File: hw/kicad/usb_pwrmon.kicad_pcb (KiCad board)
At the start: 2 copper layers, 31 parts, among them J1 ARM_10PIN, J2 USB_MALE_A, J3 USB_MICRO_B, J4 USB_FEMALE_A, SW1 SW_PUSH, U1 AD8293G80, U2 MKL24Z64VFM4

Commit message: - save
Former-commit-id: cf66670b65a8a882cb1622ef3f0bdfdf1408bc8a
Former-commit-id: 7a3e1ac5155b1945f7744ff238828485aaafe397
Former-commit-id: 743023cbd18d02b8dd289aac27cf0dd998f1e37a
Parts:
- moved J_2 6.27 mm to (85.9, 23.9)
- moved U2 5.92 mm to (91.9, 31.2), turned to 45 degrees
- moved U1 2.03 mm to (82.5, 28.7)
- moved R6 0.80 mm to (84.1, 35.1)
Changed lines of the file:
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@@
     (mod_text_size 1.5 1.5)
     (mod_text_width 0.15)
-    (pad_size 1.6 1.4)
-    (pad_drill 0)
+    (pad_size 3.4 3.4)
+    (pad_drill 2)
     (pad_to_mask_clearance 0.2)
     (aux_axis_origin 0 0)
@@
   )
   (module sot23-8 (layer F.Cu)
-    (at 84.582 28.702)
+    (at 82.55 28.702)
     (fp_text reference U1 (at 1.651 -1.397) (layer F.SilkS)
       (effects (font (size 0.75 0.75) (thickness 0.12)))
@@
   )
   (module oled_fpc_30 (layer F.Cu)
-    (at 91.694 26.162)
+    (at 85.852 23.876)
     (fp_text reference J_2 (at 0 3) (layer F.SilkS)
       (effects (font (size 0.75 0.75) (thickness 0.12)))
@@
   )
   (module MKL24Z64VFM4 (layer F.Cu)
-    (at 94.996 36.322)
-    (fp_text reference U2 (at 0 -6) (layer F.SilkS)
-      (effects (font (size 0.75 0.75) (thickness 0.12)))
-    )
-    (fp_text value MKL24Z64VFM4 (at 0 5) (layer F.SilkS) hide
+    (at 91.948 31.242 45)
+    (fp_text reference U2 (at 0 -6 45) (layer F.SilkS)
+      (effects (font (size 0.75 0.75) (thickness 0.12)))
+    )
+    (fp_text value MKL24Z64VFM4 (at 0 5 45) (layer F.SilkS) hide
       (effects (font (size 1 1) (thickness 0.15)))
     )
-    (pad 1 smd rect (at -2.475 -1.75) (size 0.85 0.3)
+    (pad 1 smd rect (at -2.475 -1.75 45) (size 0.85 0.3)
       (layers F.Cu F.Paste F.Mask)
       (net 36 Net-<U2-Pad1>)
     )
-    (pad 2 smd rect (at -2.475 -1.25) (size 0.85 0.3)
-      (layers F.Cu F.Paste F.Mask)
-      (net 7 GND)
-    )
-    (pad 3 smd rect (at -2.475 -0.75) (size 0.85 0.3)
+    (pad 2 smd rect (at -2.475 -1.25 45) (size 0.85 0.3)
+      (layers F.Cu F.Paste F.Mask)
+      (net 7 GND)
+    )
+    (pad 3 smd rect (at -2.475 -0.75 45) (size 0.85 0.3)
       (layers F.Cu F.Paste F.Mask)
       (net 28 Net-<R4-Pad2>)
     )
-    (pad 4 smd rect (at -2.475 -0.25) (size 0.85 0.3)
+    (pad 4 smd rect (at -2.475 -0.25 45) (size 0.85 0.3)
       (layers F.Cu F.Paste F.Mask)
       (net 29 Net-<R5-Pad2>)
     )
-    (pad 5 smd rect (at -2.475 0.25) (size 0.85 0.3)
+    (pad 5 smd rect (at -2.475 0.25 45) (size 0.85 0.3)
       (layers F.Cu F.Paste F.Mask)
       (net 2 +3.3v)
     )
-    (pad 6 smd rect (at -2.475 0.75) (size 0.85 0.3)
+    (pad 6 smd rect (at -2.475 0.75 45) (size 0.85 0.3)
       (layers F.Cu F.Paste F.Mask)
       (net 47 USB_VBUS)
     )
-    (pad 7 smd rect (at -2.475 1.25) (size 0.85 0.3)
+    (pad 7 smd rect (at -2.475 1.25 45) (size 0.85 0.3)
       (layers F.Cu F.Paste F.Mask)
       (net 2 +3.3v)
     )
-    (pad 8 smd rect (at -2.475 1.75) (size 0.85 0.3)
-      (layers F.Cu F.Paste F.Mask)
-      (net 7 GND)
-    )
-    (pad 17 smd rect (at 2.475 1.75) (size 0.85 0.3)
+    (pad 8 smd rect (at -2.475 1.75 45) (size 0.85 0.3)
+      (layers F.Cu F.Paste F.Mask)
+      (net 7 GND)
+    )
+    (pad 17 smd rect (at 2.475 1.75 45) (size 0.85 0.3)
       (layers F.Cu F.Paste F.Mask)
       (net 34 Net-<U2-Pad17>)
     )
-    (pad 18 smd rect (at 2.475 1.25) (size 0.85 0.3)
+    (pad 18 smd rect (at 2.475 1.25 45) (size 0.85 0.3)
       (layers F.Cu F.Paste F.Mask)
       (net 35 Net-<U2-Pad18>)
     )
-    (pad 19 smd rect (at 2.475 0.75) (size 0.85 0.3)
+    (pad 19 smd rect (at 2.475 0.75 45) (size 0.85 0.3)
       (layers F.Cu F.Paste F.Mask)
       (net 9 NRESET)
     )
-    (pad 20 smd rect (at 2.475 0.25) (size 0.85 0.3)
+    (pad 20 smd rect (at 2.475 0.25 45) (size 0.85 0.3)
       (layers F.Cu F.Paste F.Mask)
       (net 37 Net-<U2-Pad20>)
     )
-    (pad 21 smd rect (at 2.475 -0.25) (size 0.85 0.3)
+    (pad 21 smd rect (at 2.475 -0.25 45) (size 0.85 0.3)
       (layers F.Cu F.Paste F.Mask)
       (net 38 Net-<U2-Pad21>)
     )
-    (pad 22 smd rect (at 2.475 -0.75) (size 0.85 0.3)
+    (pad 22 smd rect (at 2.475 -0.75 45) (size 0.85 0.3)
       (layers F.Cu F.Paste F.Mask)
       (net 39 Net-<U2-Pad22>)
     )
-    (pad 23 smd rect (at 2.475 -1.25) (size 0.85 0.3)
+    (pad 23 smd rect (at 2.475 -1.25 45) (size 0.85 0.3)
       (layers F.Cu F.Paste F.Mask)
       (net 48 ~CS)
     )
-    (pad 24 smd rect (at 2.475 -1.75) (size 0.85 0.3)
+    (pad 24 smd rect (at 2.475 -1.75 45) (size 0.85 0.3)
       (layers F.Cu F.Paste F.Mask)
       (net 49 ~RST)
     )
-    (pad 9 smd rect (at -1.75 2.475) (size 0.3 0.85)
+    (pad 9 smd rect (at -1.75 2.475 45) (size 0.3 0.85)
       (layers F.Cu F.Paste F.Mask)
       (net 30 Net-<R7-Pad2>)
     )
-    (pad 10 smd rect (at -1.25 2.475) (size 0.3 0.85)
+    (pad 10 smd rect (at -1.25 2.475 45) (size 0.3 0.85)
       (layers F.Cu F.Paste F.Mask)
       (net 43 SWCLK)
     )
-    (pad 11 smd rect (at -0.75 2.475) (size 0.3 0.85)
+    (pad 11 smd rect (at -0.75 2.475 45) (size 0.3 0.85)
       (layers F.Cu F.Paste F.Mask)
       (net 18 Net-<D1-Pad1>)
     )
-    (pad 12 smd rect (at -0.25 2.475) (size 0.3 0.85)
+    (pad 12 smd rect (at -0.25 2.475 45) (size 0.3 0.85)
       (layers F.Cu F.Paste F.Mask)
       (net 32 Net-<U2-Pad12>)
     )
-    (pad 13 smd rect (at 0.25 2.475) (size 0.3 0.85)
+    (pad 13 smd rect (at 0.25 2.475 45) (size 0.3 0.85)
       (layers F.Cu F.Paste F.Mask)
       (net 44 SWDIO)
     )
-    (pad 14 smd rect (at 0.75 2.475) (size 0.3 0.85)
+    (pad 14 smd rect (at 0.75 2.475 45) (size 0.3 0.85)
       (layers F.Cu F.Paste F.Mask)
       (net 33 Net-<U2-Pad14>)
     )
-    (pad 15 smd rect (at 1.25 2.475) (size 0.3 0.85)
+    (pad 15 smd rect (at 1.25 2.475 45) (size 0.3 0.85)
       (layers F.Cu F.Paste F.Mask)
       (net 2 +3.3v)
     )
-    (pad 16 smd rect (at 1.75 2.475) (size 0.3 0.85)
-      (layers F.Cu F.Paste F.Mask)
-      (net 7 GND)
-    )
-    (pad 25 smd rect (at 1.75 -2.475) (size 0.3 0.85)
+    (pad 16 smd rect (at 1.75 2.475 45) (size 0.3 0.85)
+      (layers F.Cu F.Paste F.Mask)
+      (net 7 GND)
+    )
+    (pad 25 smd rect (at 1.75 -2.475 45) (size 0.3 0.85)
       (layers F.Cu F.Paste F.Mask)
       (net 6 DC/I2X_SA0)
     )
-    (pad 26 smd rect (at 1.25 -2.475) (size 0.3 0.85)
+    (pad 26 smd rect (at 1.25 -2.475 45) (size 0.3 0.85)
       (layers F.Cu F.Paste F.Mask)
       (net 4 D0/SPI_SCLK/I2C_SCK)
     )
-    (pad 27 smd rect (at 0.75 -2.475) (size 0.3 0.85)
+    (pad 27 smd rect (at 0.75 -2.475 45) (size 0.3 0.85)
       (layers F.Cu F.Paste F.Mask)
       (net 5 D1/SPI_SDIN/I2C_SDA)
     )
-    (pad 28 smd rect (at 0.25 -2.475) (size 0.3 0.85)
+    (pad 28 smd rect (at 0.25 -2.475 45) (size 0.3 0.85)
       (layers F.Cu F.Paste F.Mask)
       (net 40 Net-<U2-Pad28>)
     )
-    (pad 29 smd rect (at -0.25 -2.475) (size 0.3 0.85)
+    (pad 29 smd rect (at -0.25 -2.475 45) (size 0.3 0.85)
       (layers F.Cu F.Paste F.Mask)
       (net 31 Net-<SW1-Pad2>)
     )
-    (pad 30 smd rect (at -0.75 -2.475) (size 0.3 0.85)
+    (pad 30 smd rect (at -0.75 -2.475 45) (size 0.3 0.85)
       (layers F.Cu F.Paste F.Mask)
       (net 41 Net-<U2-Pad30>)
     )
-    (pad 31 smd rect (at -1.25 -2.475) (size 0.3 0.85)
+    (pad 31 smd rect (at -1.25 -2.475 45) (size 0.3 0.85)
       (layers F.Cu F.Paste F.Mask)
       (net 3 ADC_OUT)
     )
-    (pad 32 smd rect (at -1.75 -2.475) (size 0.3 0.85)
+    (pad 32 smd rect (at -1.75 -2.475 45) (size 0.3 0.85)
       (layers F.Cu F.Paste F.Mask)
       (net 42 Net-<U2-Pad32>)
     )
-    (pad "" thru_hole rect (at 0 0) (size 3.4 3.4) (drill 2)
+    (pad "" thru_hole rect (at 0 0 45) (size 3.4 3.4) (drill 2)
       (layers *.Cu *.Mask F.SilkS)
     )
   )
   (module lvk12 (layer F.Cu)
-    (at 84.836 35.306)
+    (at 84.074 35.052)
     (fp_text reference R6 (at 0 2.159) (layer F.SilkS)
       (effects (font (size 0.75 0.75) (thickness 0.12)))

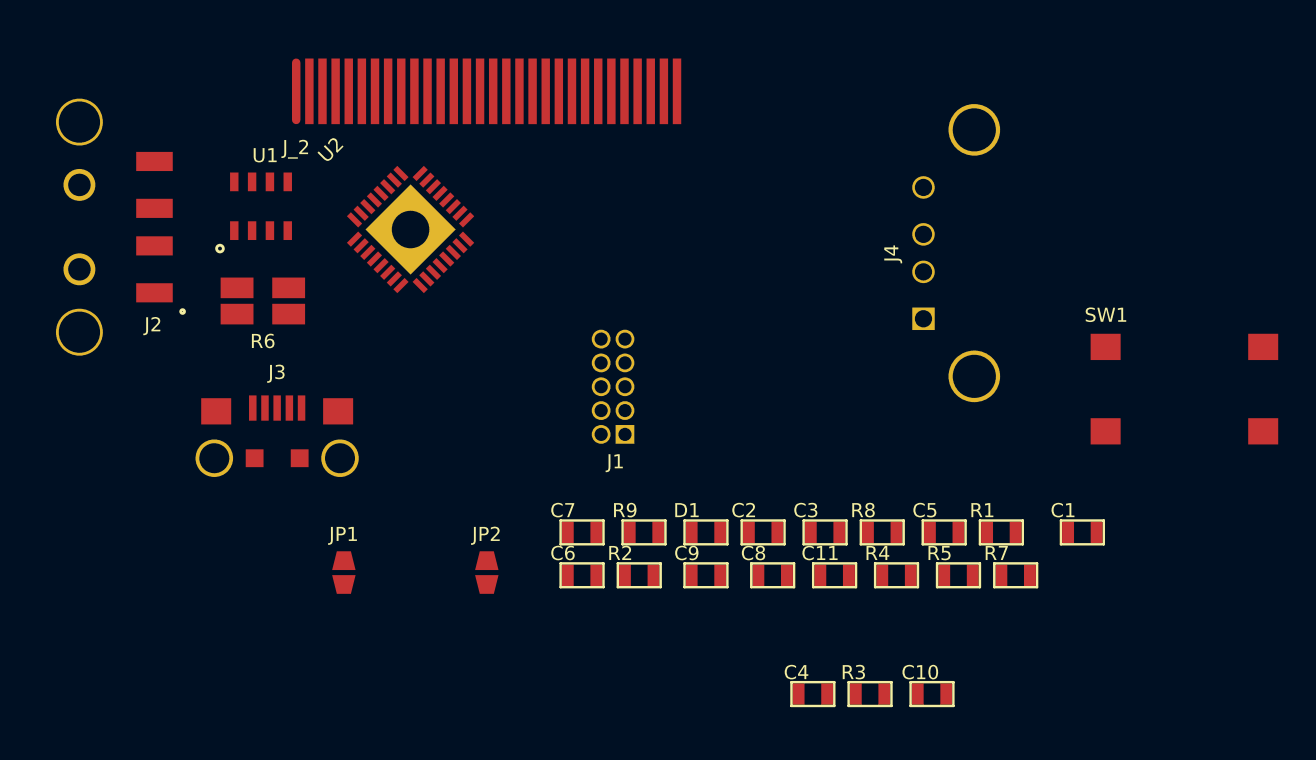
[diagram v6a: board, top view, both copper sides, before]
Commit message: - add add'l usb jumpers - save some pcb work
Former-commit-id: 4305312ec84a4c15a7d9898fff606bb72ee18eb2
Former-commit-id: 04b2ca7ae01f3977115ae03f7eda25a8efc5ed7b
Former-commit-id: 2e574d4f80fddf631c4dad79bdb68b46444f8834
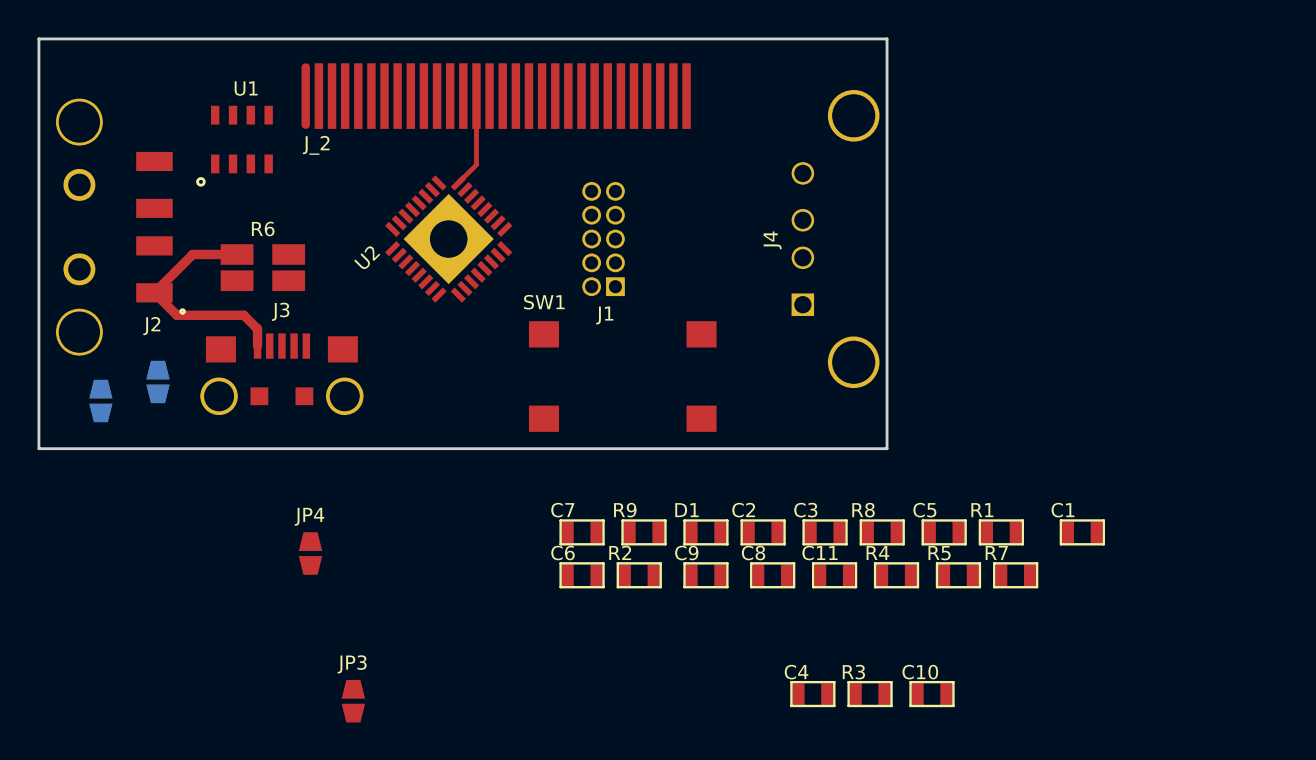
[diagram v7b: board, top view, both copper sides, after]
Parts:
- added JP3: JUMPER, jmp_small, F.Cu at (88.9, 56.4)
- added JP4: JUMPER, jmp_small, F.Cu at (86.6, 48.5)
- JP1, JP2: moved to B.Cu
- moved SW1 29.9 mm to (99.1, 36.8)
- moved JP2 22.5 mm to (75.4, 40.4)
- moved JP1 14.2 mm to (78.5, 39.4)
- moved J1 7.89 mm to (102.9, 31.8)
- moved J4 6.47 mm to (115.6, 31.8)
- moved U1 3.70 mm to (81.5, 25.1)
- moved J3 3.31 mm to (85.1, 40.1)
- moved U2 2.09 mm to (94.0, 31.8)
- moved R6 1.78 mm to (84.1, 33.3)
- moved J_2 0.57 mm to (86.4, 24.1)
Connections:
- net Net-<C1-Pad2> renamed N-0000046
- net Net-<C2-Pad1> renamed N-0000042
- net Net-<C2-Pad2> renamed N-0000049
- net Net-<C3-Pad1> renamed N-0000041
- net Net-<C3-Pad2> renamed N-0000048
- net Net-<C6-Pad2> renamed N-0000045
- net Net-<C9-Pad1> renamed N-0000010
- net Net-<C9-Pad2> renamed N-000009
- net Net-<D1-Pad1> renamed N-0000012
- net Net-<D1-Pad2> renamed N-0000013
- net Net-<J4-Pad1> renamed N-0000037
- net Net-<J_2-Pad26> renamed N-0000047
- net Net-<R2-Pad1> renamed N-0000011
- net Net-<R4-Pad2> renamed N-000006
- net Net-<R5-Pad2> renamed N-000007
- net Net-<R7-Pad2> renamed N-0000028
- net Net-<SW1-Pad2> renamed N-0000020
- J1 pad 6: Net-<J1-Pad6> -> (no net)
- J1 pad 7: Net-<J1-Pad7> -> (no net)
- J1 pad 8: Net-<J1-Pad8> -> (no net)
- J3 pad 4: Net-<J3-Pad4> -> (no net)
- J4 pad 2: USB_DP -> (no net)
- J4 pad 3: USB_DM -> TRGT_USB_DM
- J_2 pad 7: Net-<J_2-Pad7> -> (no net)
- U2 pad 1: Net-<U2-Pad1> -> (no net)
- U2 pad 12: Net-<U2-Pad12> -> (no net)
- U2 pad 14: Net-<U2-Pad14> -> (no net)
- U2 pad 17: Net-<U2-Pad17> -> (no net)
- U2 pad 18: Net-<U2-Pad18> -> (no net)
- U2 pad 20: Net-<U2-Pad20> -> (no net)
- U2 pad 21: Net-<U2-Pad21> -> (no net)
- U2 pad 22: Net-<U2-Pad22> -> (no net)
- U2 pad 28: Net-<U2-Pad28> -> (no net)
- U2 pad 30: Net-<U2-Pad30> -> (no net)
- U2 pad 32: Net-<U2-Pad32> -> (no net)
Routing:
- net USB_VBUS: track 0.00 -> 12.5 mm
- net ~RST: track 0.00 -> 5.03 mm
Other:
- board outline added: 45.2 x 21.8 mm
- net class Default: clearance 0.254 -> 0.1524
- rule trace_clearance: 0.254 -> 0.1524
